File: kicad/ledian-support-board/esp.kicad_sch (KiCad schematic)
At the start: 7 parts, among them J5 Conn_01x04_Pin

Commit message: kicad: ledian-support-board: added titles to all pages
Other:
- title: (none) -> ESP
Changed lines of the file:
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@@
 (kicad_sch (version 20230121) (generator eeschema)
   (paper "A4")
+  (title_block
+    (title "ESP")
+  )
   (junction (at 104.14 95.25) (diameter 0) (color 0 0 0 0)
   )

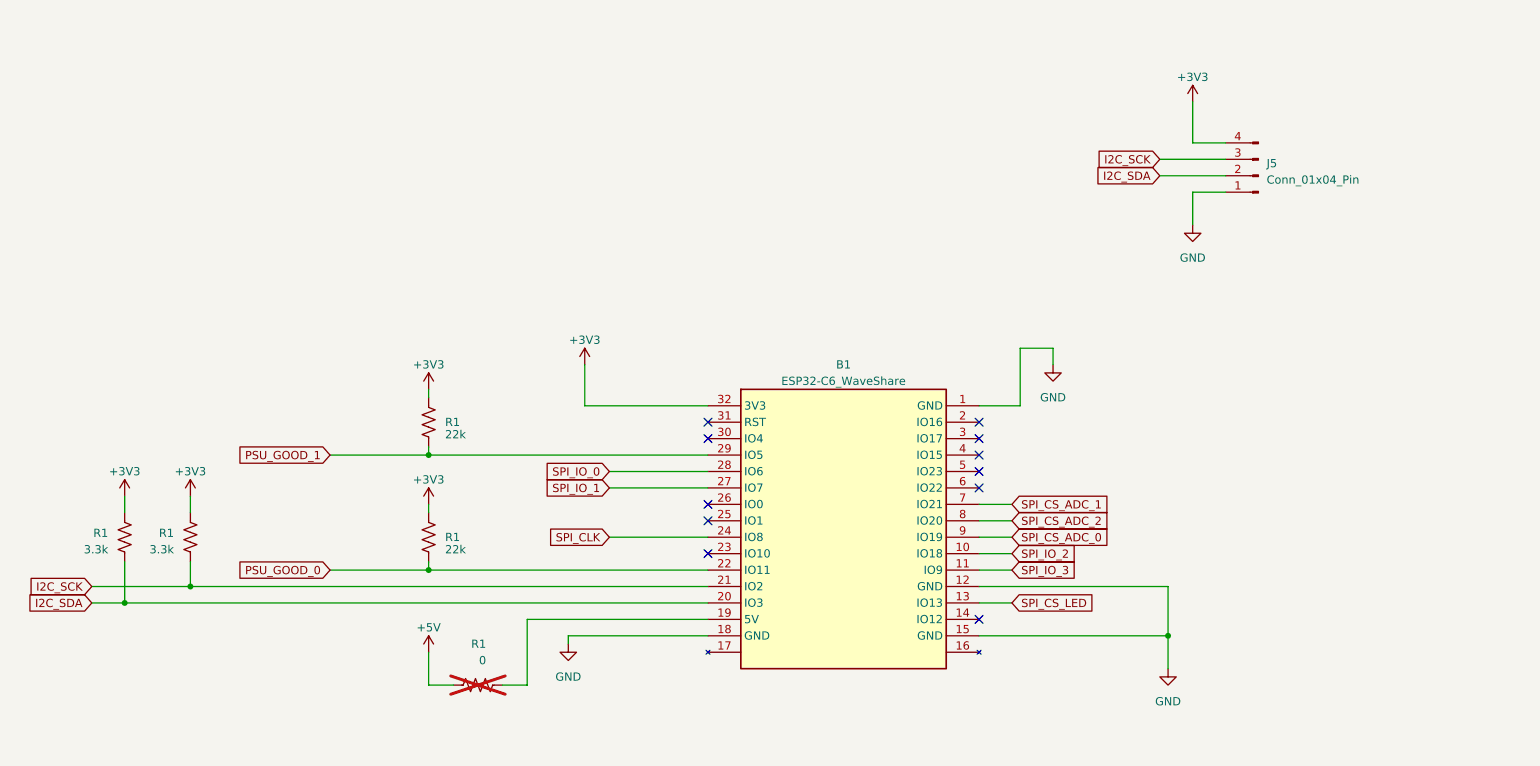
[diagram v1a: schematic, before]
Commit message: kicad: ledian-support-board: added some comments to parts of the circuit
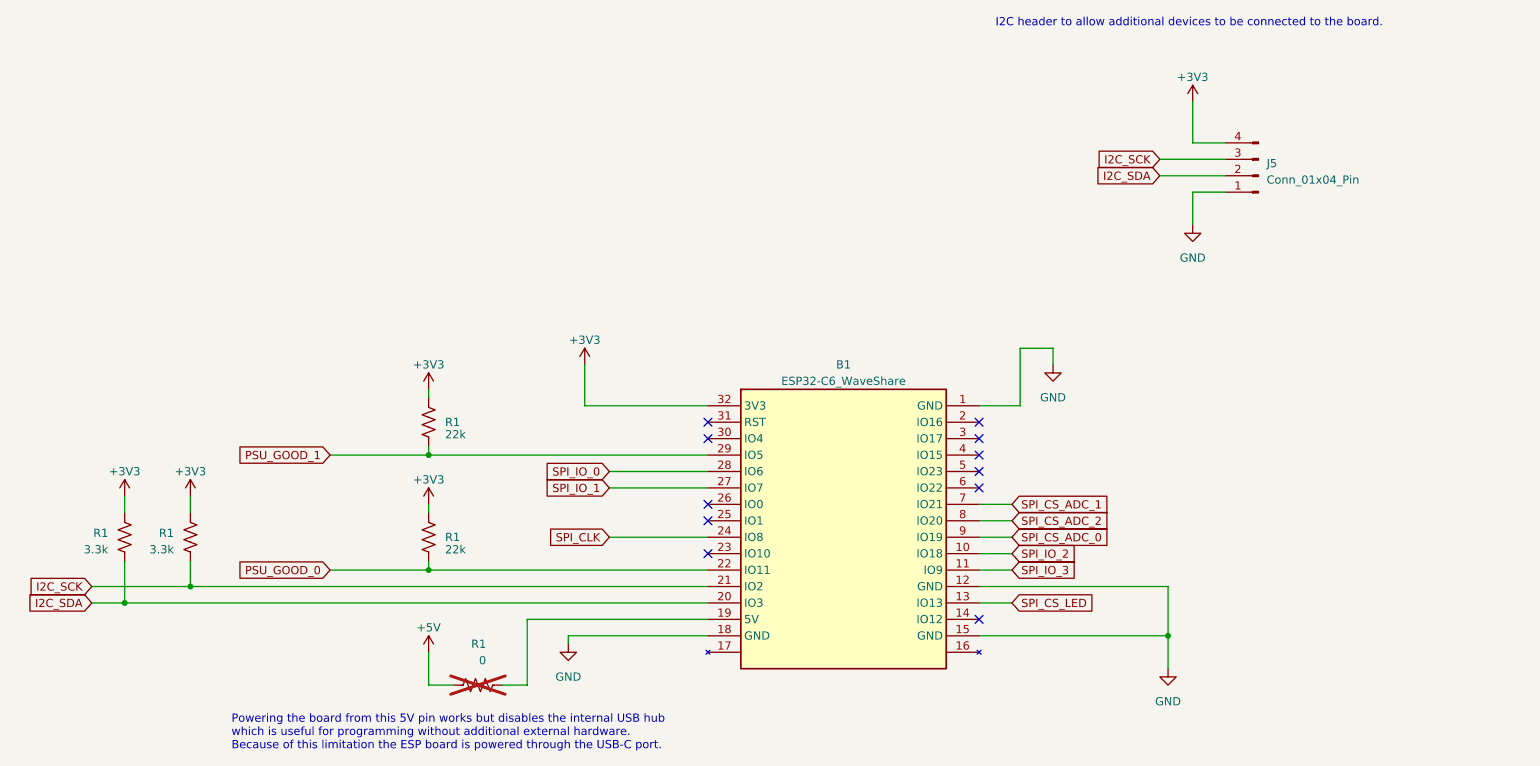
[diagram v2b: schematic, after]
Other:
- note added: "I2C header to allow additional devices to be connected to the board."
- note added: "Powering the board from this 5V pin works but disables the internal USB hub which is useful for programming without additional external hardware. Because of this limitation the ESP board is powered through the USB-C port."
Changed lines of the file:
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@@
     (stroke (width 0) (type default))
+  )
+  (text "Powering the board from this 5V pin works but disables the internal USB hub\nwhich is useful for programming without additional external hardware.\nBecause of this limitation the ESP board is powered through the USB-C port."
+    (at 73.66 140.97 0)
+    (effects (font (size 1.27 1.27)) (justify left bottom))
+  )
+  (text "I2C header to allow additional devices to be connected to the board."
+    (at 191.77 29.21 0)
+    (effects (font (size 1.27 1.27)) (justify left bottom))
   )
   (global_label "I2C_SCK" (shape input) (at 217.17 49.53 180) (fields_autoplaced)
